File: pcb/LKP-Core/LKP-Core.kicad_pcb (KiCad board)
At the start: 2 copper layers, 41 x 34 mm, 31 parts, among them J1 Intercon L, J2 Intercon R, J3 Power JST PH, J4 IO, J5 SWD, J6 WS281x, U1 CY8C4246AZI-M445

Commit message: MOAR VIAS
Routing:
- net GND: vias 55 -> 60
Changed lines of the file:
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@@
     (thickness 1.6)
     (drawings 13)
-    (tracks 482)
+    (tracks 487)
     (zones 0)
     (modules 31)
@@
   (segment (start 137.412087 93.737087) (end 137.524219 93.737087) (width 0.5) (layer F.Cu) (net 1) (status 30))
   (via (at 157.322767 108.610232) (size 0.8) (drill 0.4) (layers F.Cu B.Cu) (net 1))
+  (via (at 148.875 82.5) (size 0.8) (drill 0.4) (layers F.Cu B.Cu) (net 1))
+  (via (at 148.875 80) (size 0.8) (drill 0.4) (layers F.Cu B.Cu) (net 1))
+  (via (at 137.875 84.5) (size 0.8) (drill 0.4) (layers F.Cu B.Cu) (net 1))
+  (via (at 149.375 84) (size 0.8) (drill 0.4) (layers F.Cu B.Cu) (net 1))
+  (via (at 151.875 84) (size 0.8) (drill 0.4) (layers F.Cu B.Cu) (net 1))
   (segment (start 141.318153 91.356847) (end 142.418153 92.456847) (width 0.5) (layer B.Cu) (net 2) (status 30))
   (segment (start 142.340678 94.526338) (end 141.344672 93.530332) (width 0.2) (layer F.Cu) (net 2) (status 10))

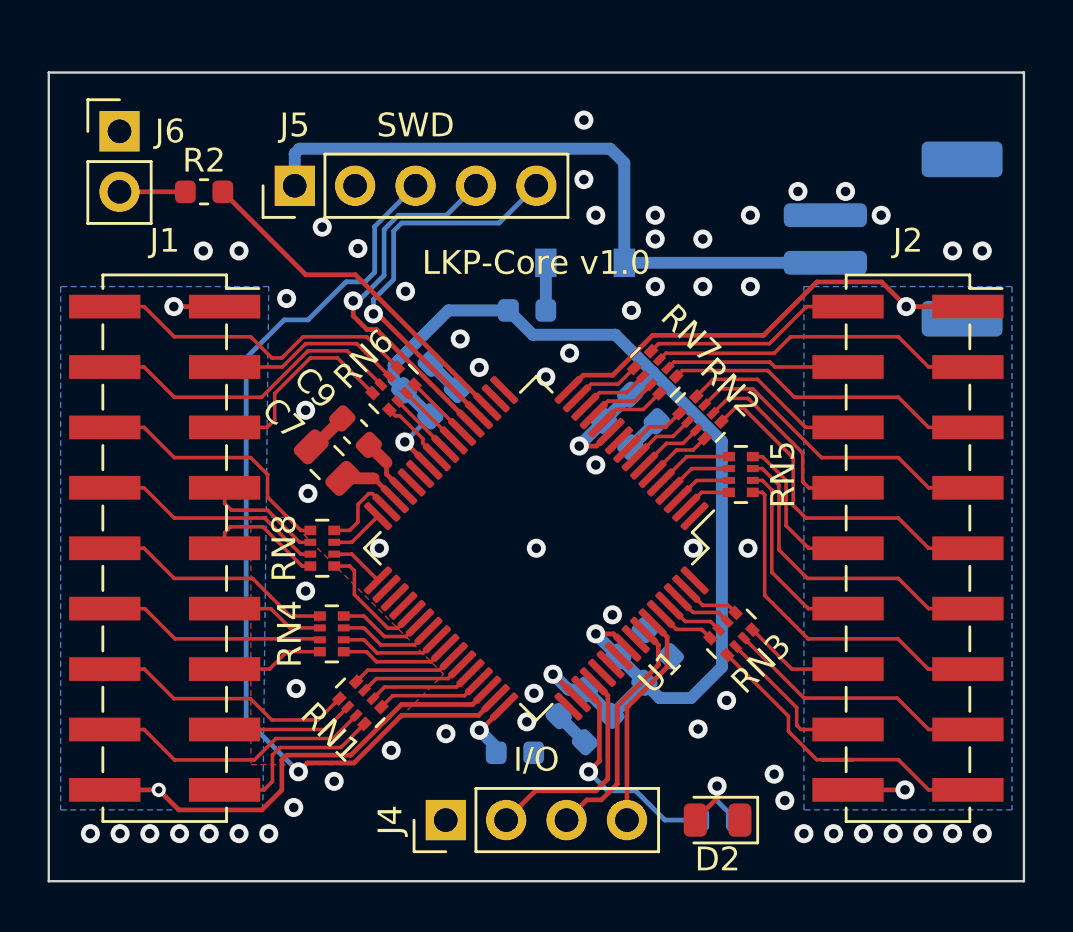
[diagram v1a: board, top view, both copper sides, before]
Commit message: Add resistors for shield
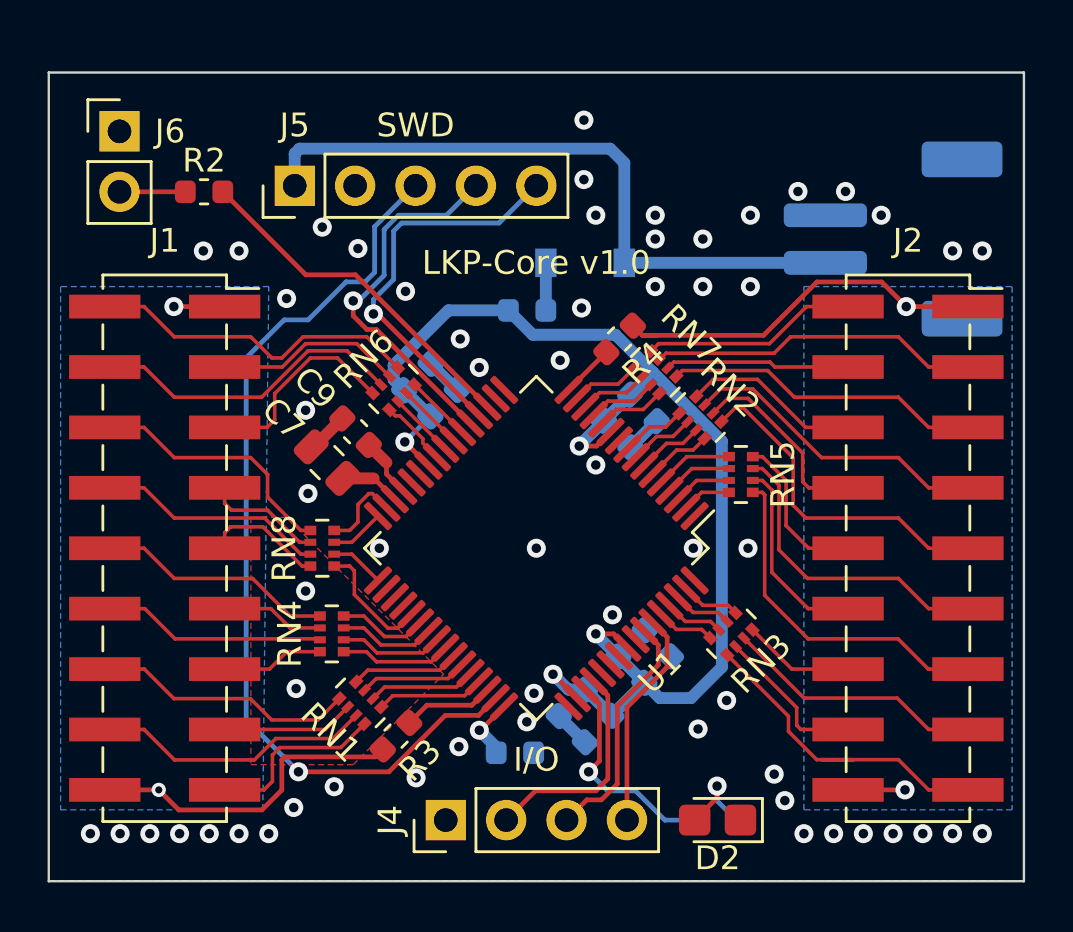
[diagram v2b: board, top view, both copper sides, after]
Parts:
- added R3: 560, Resistor_SMD:R_0603_1608Metric, F.Cu at (141.0, 105.9)
- added R4: 560, Resistor_SMD:R_0603_1608Metric, F.Cu at (150.4, 89.2)
- D2: footprint LED_SMD:LED_0805_2012Metric -> LED_SMD:LED_0805_2012Metric_Castellated
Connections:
- U1 pad 16: /S1_SH -> Net-(R4-Pad2)
- U1 pad 46: /S0_SH -> Net-(R3-Pad1)
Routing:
- net /S0_SH: track 21.4 -> 16.0 mm
- net Net-(R3-Pad1): track 0.00 -> 3.86 mm
- net /S1_SH: track 21.5 -> 18.5 mm
- net Net-(R4-Pad2): track 0.00 -> 2.25 mm
- net GND: vias 60 -> 59
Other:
- rule pad_to_mask_clearance: 0.051 -> 0.05
- rule solder_mask_min_width: 0.25 -> 0.0762

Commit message: Switch to through hole headers and add a capacitor for good luck
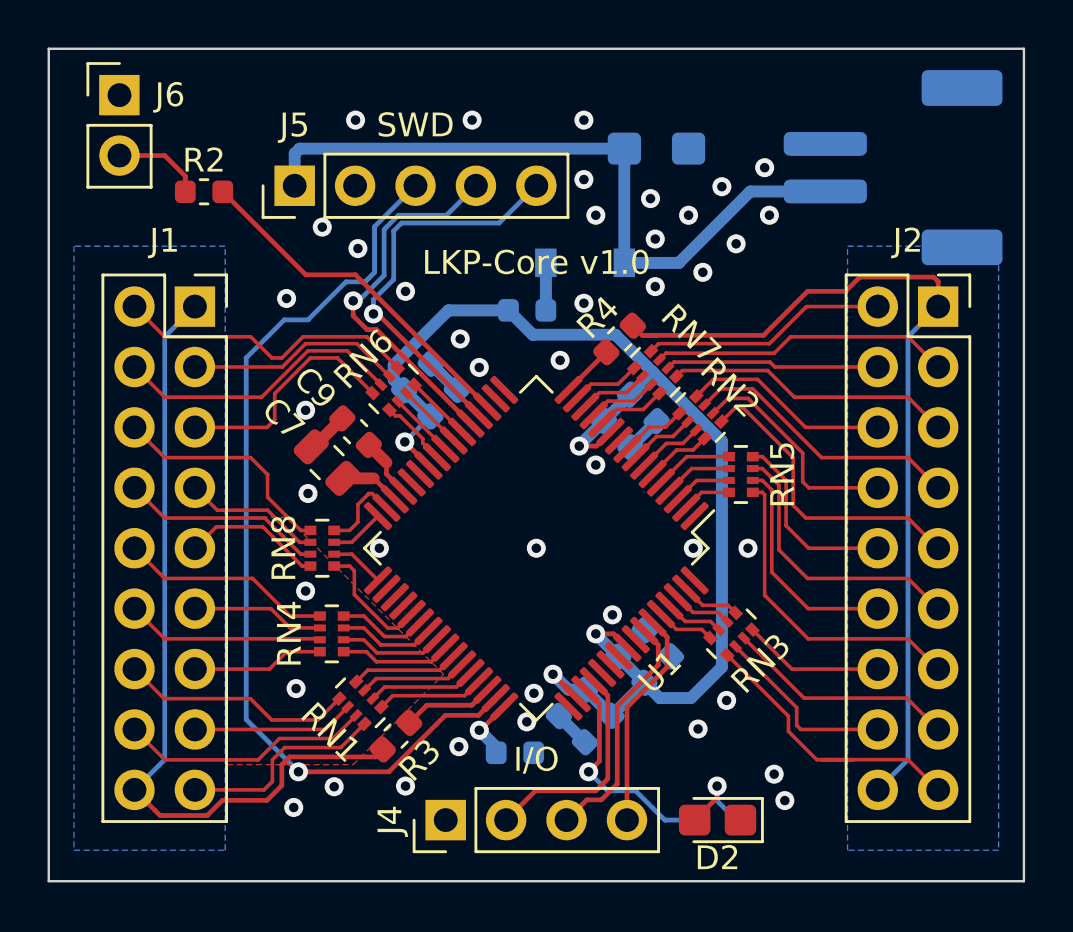
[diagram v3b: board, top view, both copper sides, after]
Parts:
- added C12: 10uF, Capacitor_Tantalum_SMD:CP_EIA-3216-18_Kemet-A, B.Cu at (151.9, 81.2)
- J1, J2: footprint Connector_PinSocket_2.54mm:PinSocket_2x09_P2.54mm_Vertical_SMD -> Connector_PinSocket_2.54mm:PinSocket_2x09_P2.54mm_Vertical
- moved J1 10.2 mm to (132.5, 87.8)
- moved J2 10.2 mm to (163.8, 87.8)
- moved J3 3.00 mm to (161.9, 82.0)
- moved J6 1.52 mm to (129.3, 79.0)
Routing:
- net /S1_SH: track 18.5 -> 37.0 mm, vias 2 -> 0
- net /S0_SH: track 16.0 -> 33.9 mm, vias 2 -> 0
- net +5V: track 28.2 -> 29.8 mm
- net /E1_4: track 14.6 -> 13.4 mm
- net /E0_4: track 11.0 -> 9.75 mm
- net /E0_10: track 9.59 -> 8.34 mm
- net /E1_8: track 14.2 -> 13.0 mm
- net /E1_7: track 6.71 -> 7.96 mm
- net /E1_6: track 13.1 -> 11.8 mm
- net /E1_5: track 8.27 -> 9.52 mm
- net /E1_3: track 4.71 -> 5.96 mm
- net /E1_2: track 11.0 -> 9.76 mm
- net /E1_15: track 9.06 -> 10.3 mm
- net /E1_14: track 13.9 -> 12.6 mm
- net /E1_12: track 13.4 -> 12.1 mm
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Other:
- board size 41 x 34 mm -> 41 x 35 mm

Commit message: Derp
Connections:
- J1 pad 10: /E0_8 -> /E0_7
- J1 pad 11: /E0_9 -> /E0_6
- J1 pad 12: /E0_10 -> /E0_5
- J1 pad 13: /E0_11 -> /E0_4
- J1 pad 14: /E0_12 -> /E0_3
- J1 pad 15: /E0_13 -> /E0_2
- J1 pad 16: /E0_14 -> /E0_1
- J1 pad 17: /E0_15 -> /E0_0
- J1 pad 2: /E0_0 -> /E0_15
- J1 pad 3: /E0_1 -> /E0_14
- J1 pad 4: /E0_2 -> /E0_13
- J1 pad 5: /E0_3 -> /E0_12
- J1 pad 6: /E0_4 -> /E0_11
- J1 pad 7: /E0_5 -> /E0_10
- J1 pad 8: /E0_6 -> /E0_9
- J1 pad 9: /E0_7 -> /E0_8
- RN1 pad 1: /E0_12 -> /E0_3
- RN1 pad 2: /E0_13 -> /E0_2
- RN1 pad 3: /E0_14 -> /E0_1
- RN1 pad 4: /E0_15 -> /E0_0
- RN1 pad 5: /S0_15 -> /S0_0
- RN1 pad 6: /S0_14 -> /S0_1
- RN1 pad 7: /S0_13 -> /S0_2
- RN1 pad 8: /S0_12 -> /S0_3
- RN4 pad 1: /E0_8 -> /E0_7
- RN4 pad 2: /E0_9 -> /E0_6
- RN4 pad 3: /E0_10 -> /E0_5
- RN4 pad 4: /E0_11 -> /E0_4
- RN4 pad 5: /S0_11 -> /S0_4
- RN4 pad 6: /S0_10 -> /S0_5
- RN4 pad 7: /S0_9 -> /S0_6
- RN4 pad 8: /S0_8 -> /S0_7
- RN6 pad 1: /E0_0 -> /E0_15
- RN6 pad 2: /E0_1 -> /E0_14
- RN6 pad 3: /E0_2 -> /E0_13
- RN6 pad 4: /E0_3 -> /E0_12
- RN6 pad 5: /S0_3 -> /S0_12
- RN6 pad 6: /S0_2 -> /S0_13
- RN6 pad 7: /S0_1 -> /S0_14
- RN6 pad 8: /S0_0 -> /S0_15
- RN8 pad 1: /E0_4 -> /E0_11
- RN8 pad 2: /E0_5 -> /E0_10
- RN8 pad 3: /E0_6 -> /E0_9
- RN8 pad 4: /E0_7 -> /E0_8
- RN8 pad 5: /S0_7 -> /S0_8
- RN8 pad 6: /S0_6 -> /S0_9
- RN8 pad 7: /S0_5 -> /S0_10
- RN8 pad 8: /S0_4 -> /S0_11
- U1 pad 22: /S0_0 -> /S0_15
- U1 pad 23: /S0_1 -> /S0_14
- U1 pad 24: /S0_2 -> /S0_13
- U1 pad 25: /S0_3 -> /S0_12
- U1 pad 31: /S0_4 -> /S0_11
- U1 pad 32: /S0_5 -> /S0_10
- U1 pad 33: /S0_6 -> /S0_9
- U1 pad 37: /S0_7 -> /S0_8
- U1 pad 38: /S0_8 -> /S0_7
- U1 pad 39: /S0_9 -> /S0_6
- U1 pad 40: /S0_10 -> /S0_5
- U1 pad 41: /S0_11 -> /S0_4
- U1 pad 42: /S0_12 -> /S0_3
- U1 pad 43: /S0_13 -> /S0_2
- U1 pad 44: /S0_14 -> /S0_1
- U1 pad 45: /S0_15 -> /S0_0
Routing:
- net /E0_2: track 12.3 -> 6.82 mm
- net /E0_13: track 6.82 -> 12.3 mm
- net /E0_4: track 9.75 -> 5.56 mm
- net /E0_11: track 5.56 -> 9.75 mm
- net /E0_15: track 8.81 -> 12.9 mm
- net /E0_0: track 12.9 -> 8.81 mm
- net /E0_8: track 8.98 -> 5.91 mm
- net /E0_7: track 5.91 -> 8.98 mm
- net /E0_9: track 5.59 -> 8.55 mm
- net /E0_6: track 8.55 -> 5.59 mm
- net /E0_5: track 5.80 -> 8.34 mm
- net /E0_10: track 8.34 -> 5.80 mm
- net /S0_5: track 2.30 -> 4.38 mm
- net /S0_10: track 4.38 -> 2.30 mm
- net /S0_9: track 4.11 -> 2.30 mm
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
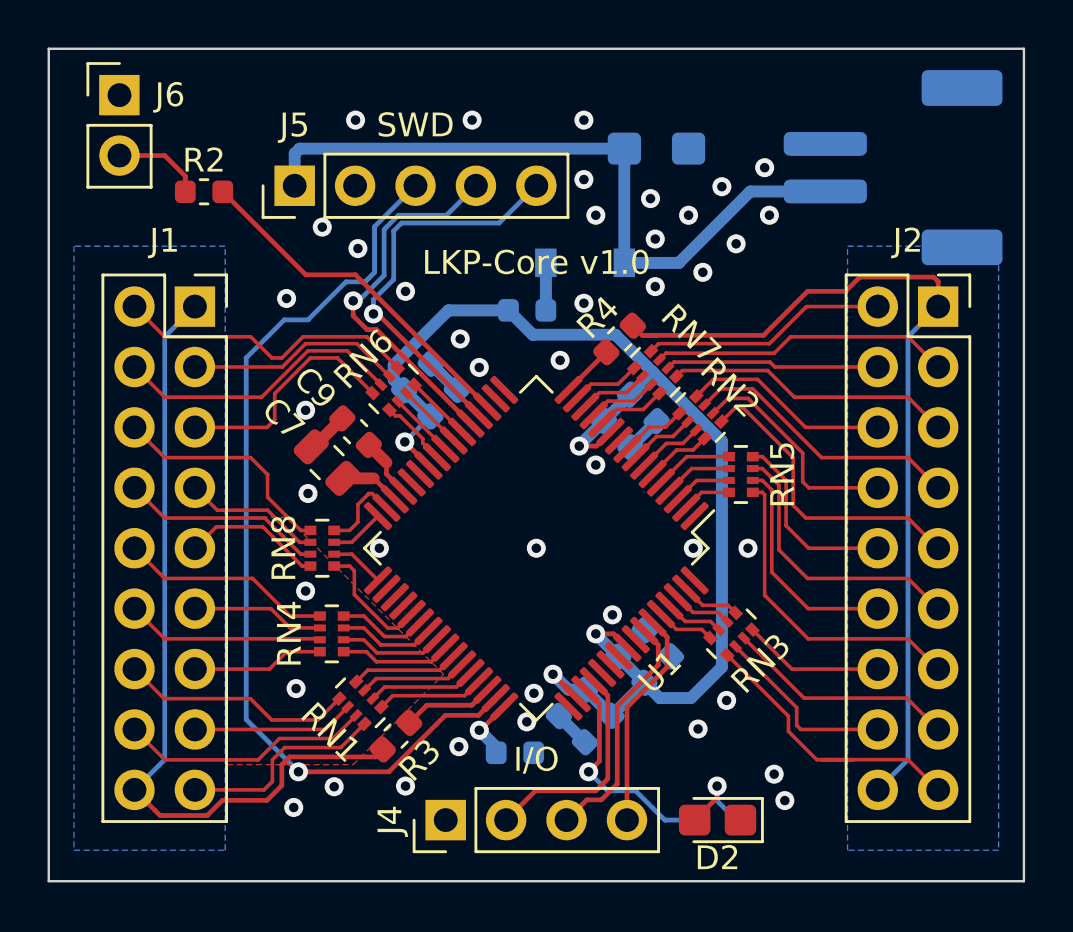
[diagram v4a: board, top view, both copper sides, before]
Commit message: Make reverse voltage protection also work with the tantalum filter cap.
Bump LKP-Core version number
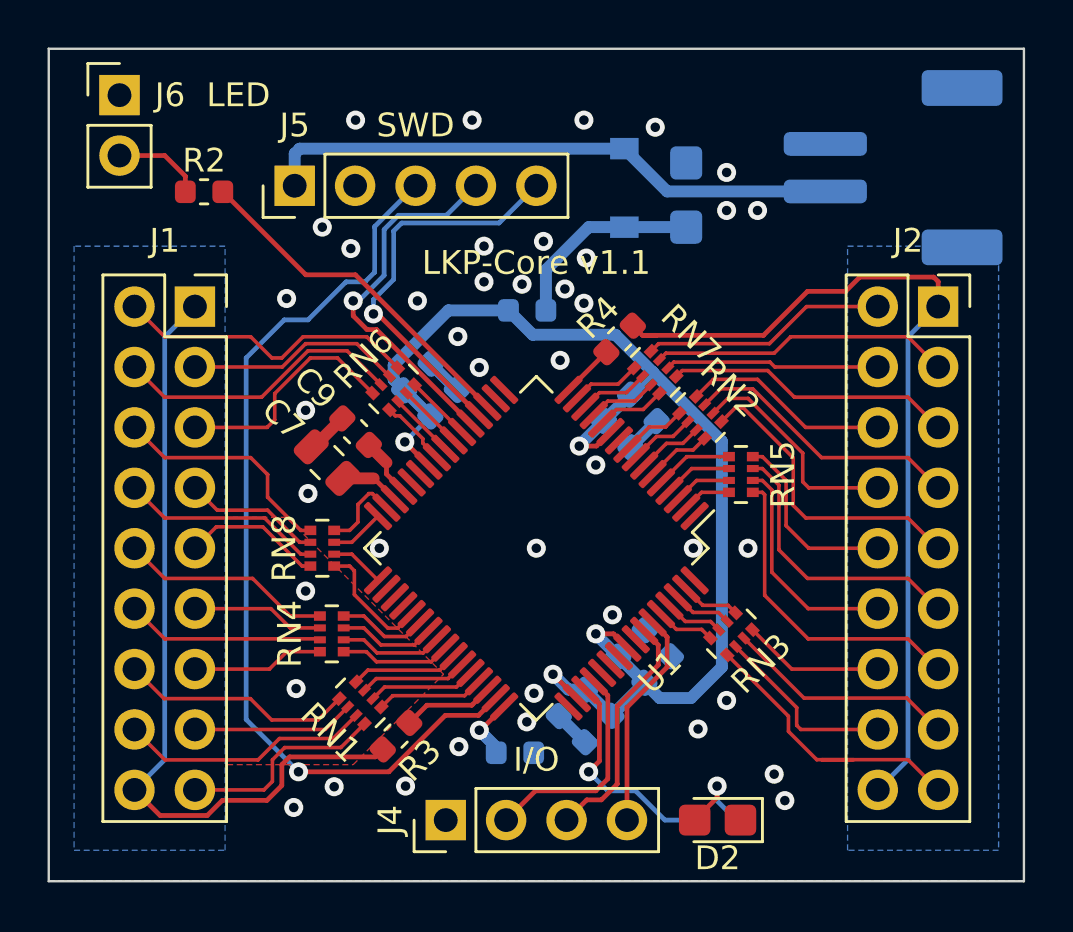
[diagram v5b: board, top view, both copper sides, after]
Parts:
- moved D1 3.56 mm to (150.6, 82.8), turned to 90 degrees
- moved C12 2.32 mm to (153.2, 83.2), turned to 90 degrees
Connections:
- C12 pad 1: +5V -> Net-(C12-Pad1)
- D1 pad 1: Net-(D1-Pad1) -> Net-(C12-Pad1)
- FB1 pad 2: Net-(D1-Pad1) -> Net-(C12-Pad1)
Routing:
- net Net-(C12-Pad1): track 0.00 -> 8.35 mm
- net +5V: track 29.8 -> 24.5 mm
- net Net-(D1-Pad1): track 2.00 -> 0.00 mm
- net GND: vias 42 -> 41
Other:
- board text added: "5V"
- board text added: "LED"
- board text added: "LKP-Core v1.1"
- board text removed: "LKP-Core v1.0"
